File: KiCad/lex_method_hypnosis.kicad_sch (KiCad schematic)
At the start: 6 parts, among them J1 Conn_02x05_Odd_Even, J2 Conn_02x05_Odd_Even

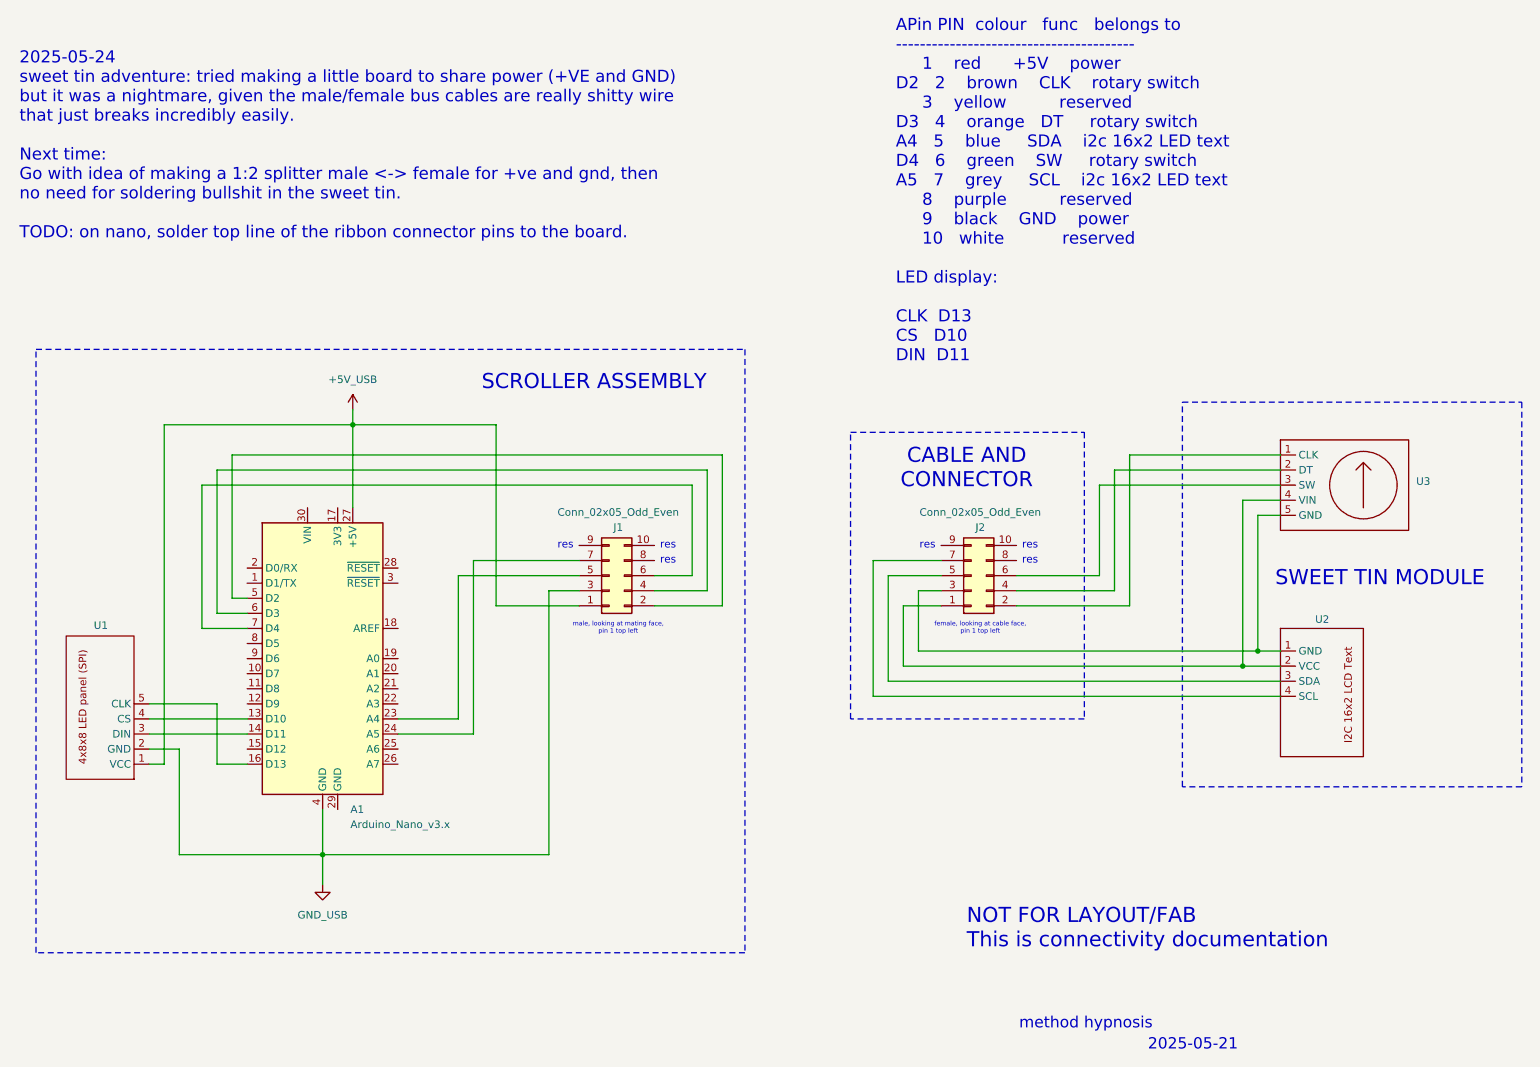
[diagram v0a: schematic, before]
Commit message: Add comments about improvements to schem
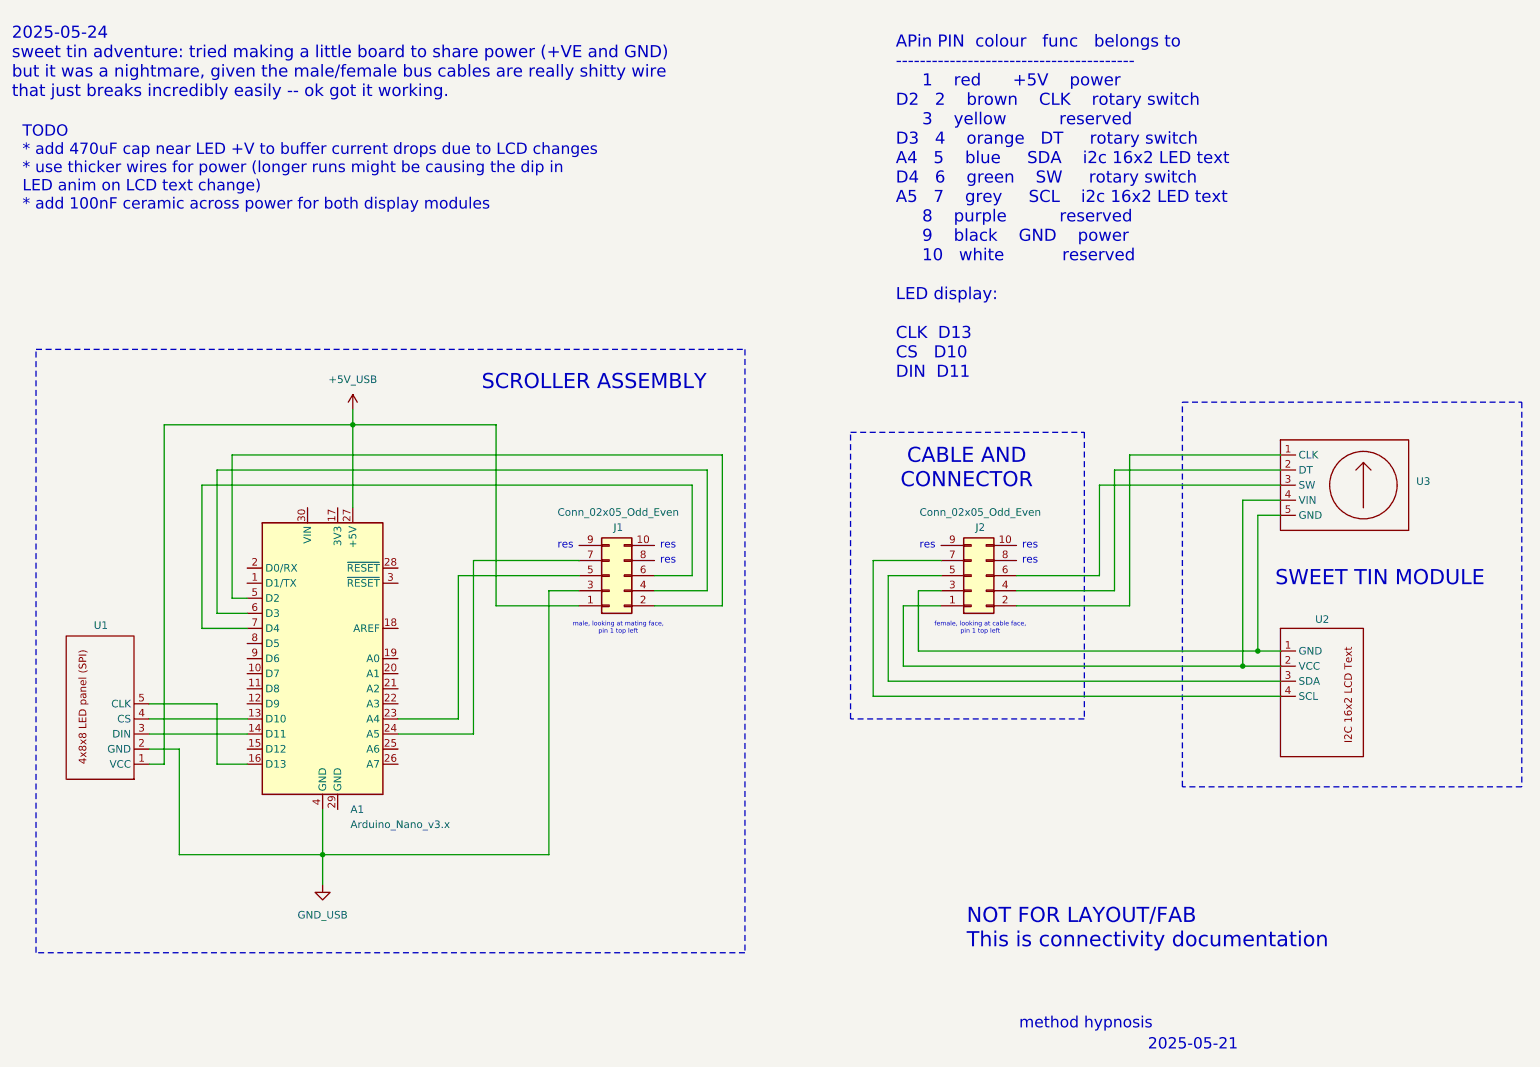
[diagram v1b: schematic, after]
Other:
- note added: "2025-05-24 sweet tin adventure: tried making a little board to share power (+VE and GND) but it was a nightmare, given the male/female bus cables are really shitty wire that just breaks incredibly easily -- ok got it working."
- note added: "TODO * add 470uF cap near LED +V to buffer current drops due to LCD changes * use thicker wires for power (longer runs might be causing the dip in LED anim on LCD text change) * add 100nF ceramic across power for both display modules"
- note removed: "2025-05-24 sweet tin adventure: tried making a little board to share power (+VE and GND) but it was a nightmare, given the male/female bus cables are really shitty wire that just breaks incredibly easily. Next time: Go with idea of making a 1:2 splitter male <-> female for +ve and gnd, then no need for soldering bullshit in the sweet tin. TODO: on nano, solder top line of the ribbon connector pin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"
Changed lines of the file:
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@@
+		)
+	)
+	(text "TODO\n* add 470uF cap near LED +V to buffer current drops due to LCD changes\n* use thicker wires for power (longer runs might be causing the dip in\nLED anim on LCD text change)\n* add 100nF ceramic across power for both display modules\n"
+		(exclude_from_sim no)
+		(at 21.844 45.72 0)
+		(effects
+			(font
+				(size 1.905 1.905)
+			)
+			(justify left)
 		)
 	)
@@
 	(text "APin PIN  colour   func   belongs to\n----------------------------------------\n     1    red      +5V    power\nD2   2    brown    CLK    rotary switch\n     3    yellow          reserved\nD3   4    orange   DT     rotary switch\nA4   5    blue     SDA    i2c 16x2 LED text\nD4   6    green    SW     rotary switch\nA5   7    grey     SCL    i2c 16x2 LED text\n     8    purple          reserved\n     9    black    GND    power\n     10   white           reserved\n\nLED display:\n\nCLK  D13\nCS   D10\nDIN  D11\n"
 		(exclude_from_sim no)
-		(at 168.91 49.53 0)
+		(at 168.91 52.324 0)
 		(effects
 			(font
@@
 		)
 	)
-	(text "2025-05-24\nsweet tin adventure: tried making a little board to share power (+VE and GND)\nbut it was a nightmare, given the male/female bus cables are really shitty wire\nthat just breaks incredibly easily. \n\nNext time:\nGo with idea of making a 1:2 splitter male <-> female for +ve and gnd, then\nno need for soldering bullshit in the sweet tin.\n\nTODO: on nano, solder top line of the ribbon connector pins to the board.\n"
+	(text "2025-05-24\nsweet tin adventure: tried making a little board to share power (+VE and GND)\nbut it was a nightmare, given the male/female bus cables are really shitty wire\nthat just breaks incredibly easily -- ok got it working."
 		(exclude_from_sim no)
-		(at 21.336 41.91 0)
+		(at 20.066 27.94 0)
 		(effects
 			(font

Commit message: Add buffer+noise caps
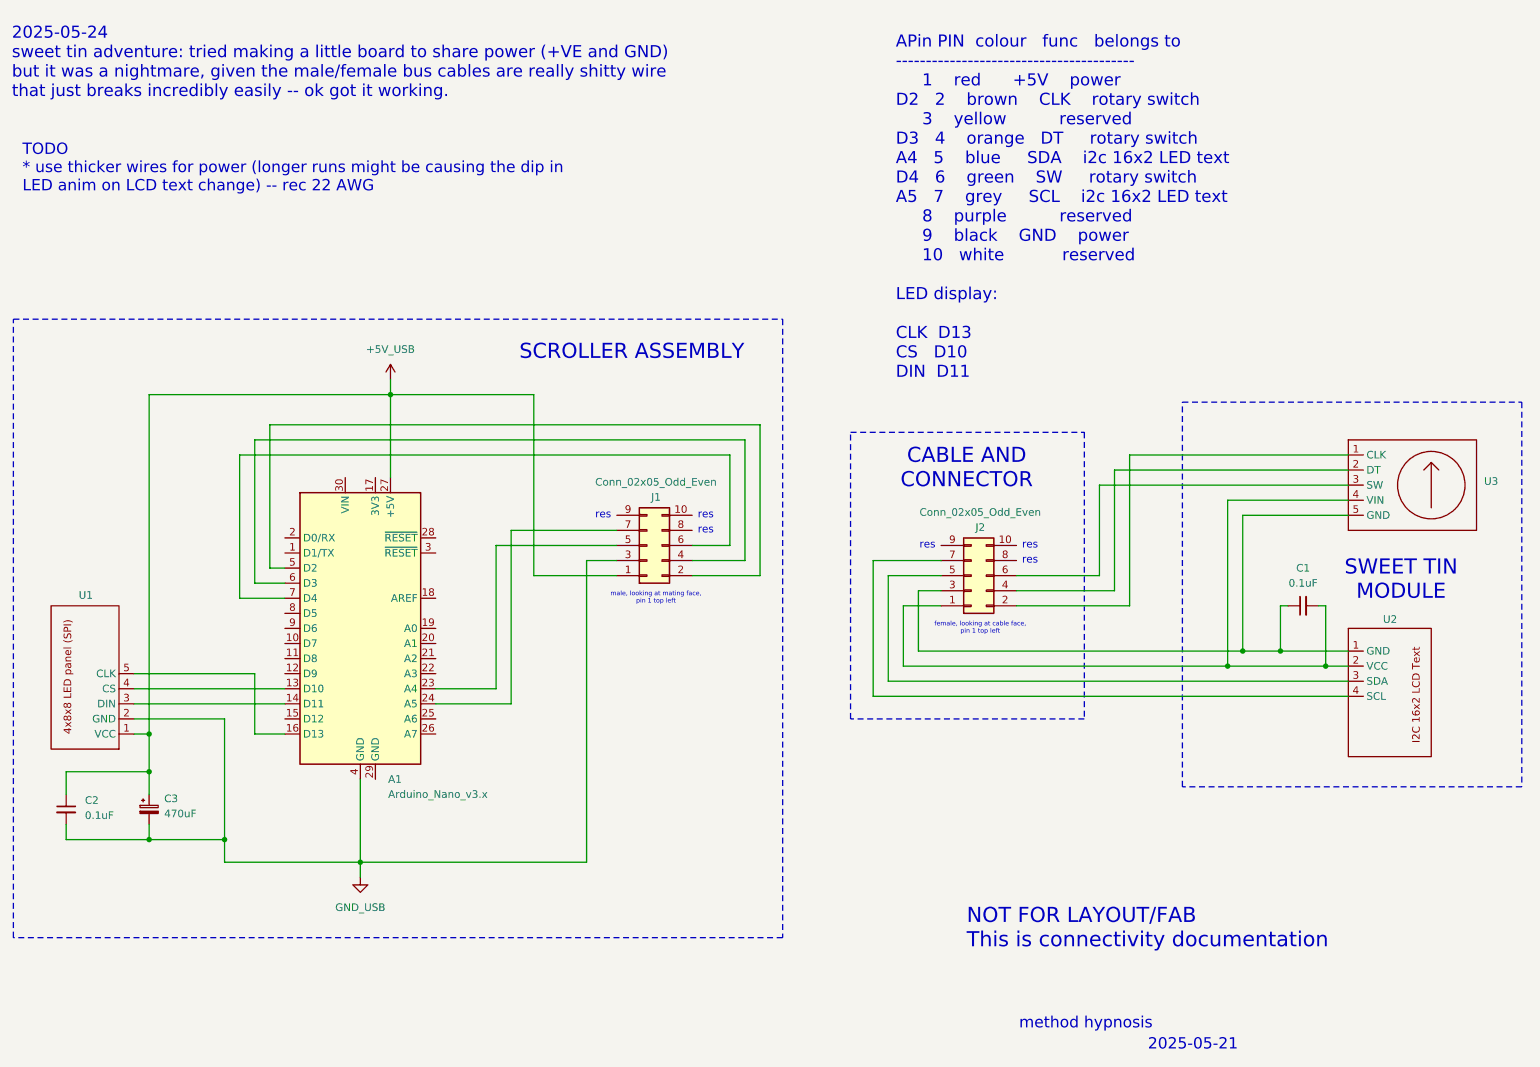
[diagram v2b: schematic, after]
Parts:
- added C1, C2: 0.1uF, symbol Device:C_Small
- added C3: 470uF, symbol Device:C_Polarized_Small
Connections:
- net +5V_USB: now also C2.1, C3.1
- net GND_USB: now also C2.2, C3.2
- net at J2.3 (Pin_3), U2.1 (GND), U3.5 (GND): now also C1.1
- net at J2.1 (Pin_1), U2.2 (VCC), U3.4 (VIN): now also C1.2
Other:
- note added: "TODO * use thicker wires for power (longer runs might be causing the dip in LED anim on LCD text change) -- rec 22 AWG"
- note removed: "TODO * add 470uF cap near LED +V to buffer current drops due to LCD changes * use thicker wires for power (longer runs might be causing the dip in LED anim on LCD text change) * add 100nF ceramic across power for both display modules"
- moved on the sheet: A1, J1, U1, U2, U3
